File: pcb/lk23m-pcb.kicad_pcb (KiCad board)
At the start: 2 copper layers, 76.2 x 119.1 mm, 59 parts, among them J1 Conn_01x02, SW1 RotaryEncoder_Switch_MP, SW10 SW_Push, SW11 SW_Push, SW12 SW_Push, SW13 SW_Push, SW14 SW_Push, SW15 SW_Push, SW16 SW_Push, SW17 SW_Push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

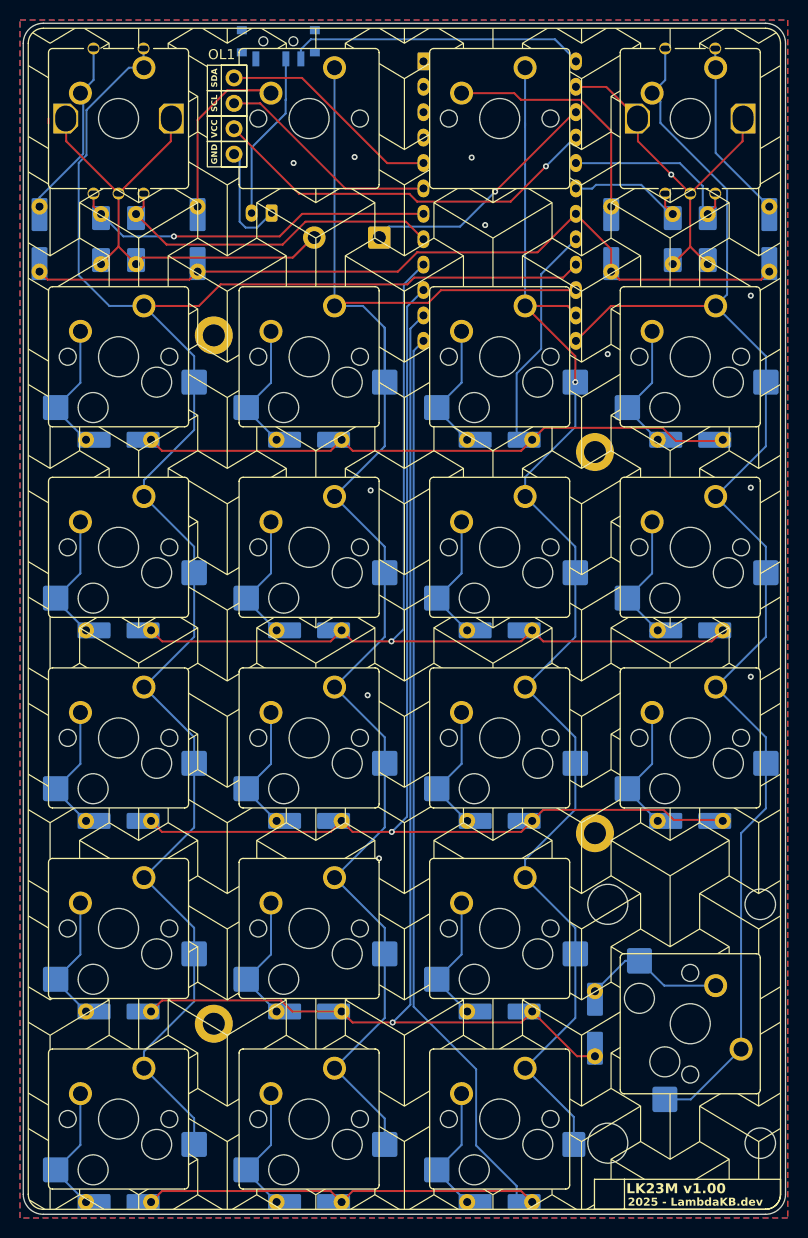
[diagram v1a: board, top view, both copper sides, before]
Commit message: Update LKBD and use new SW+Stab layout (#9)
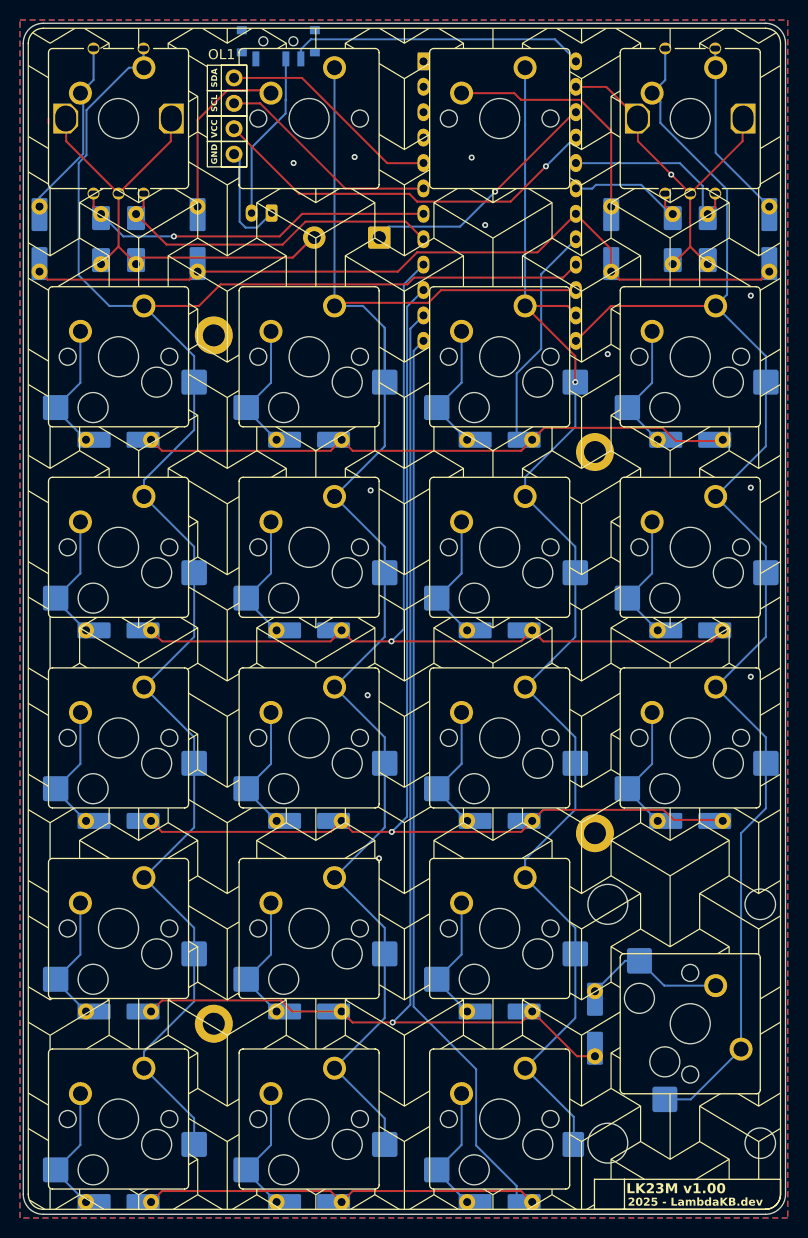
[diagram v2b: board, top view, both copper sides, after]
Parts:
- added STAB23: Stabilizer_MX_2U, LKBD_StabMX:Stabilizer_MX_2U, F.Cu at (96.7, 130.0)
- SW23: footprint LKBD_KeySwitch:SW_MX_2U_HotSwap_THT_sqSilk -> LKBD_KeySwitch:SW_MX_HotSwap_THT_sqSilk
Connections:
- SW1 pad S1: col0 -> E1S2
- SW1 pad S2: E1S2 -> col0
- SW4 pad S1: E2S1 -> col3
- SW4 pad S2: col3 -> E2S1
